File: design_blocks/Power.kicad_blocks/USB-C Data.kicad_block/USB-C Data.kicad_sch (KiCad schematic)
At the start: 7 parts, among them J12 USB_C_Receptacle_USB2.0_16P, U3 USBLC6-2P6

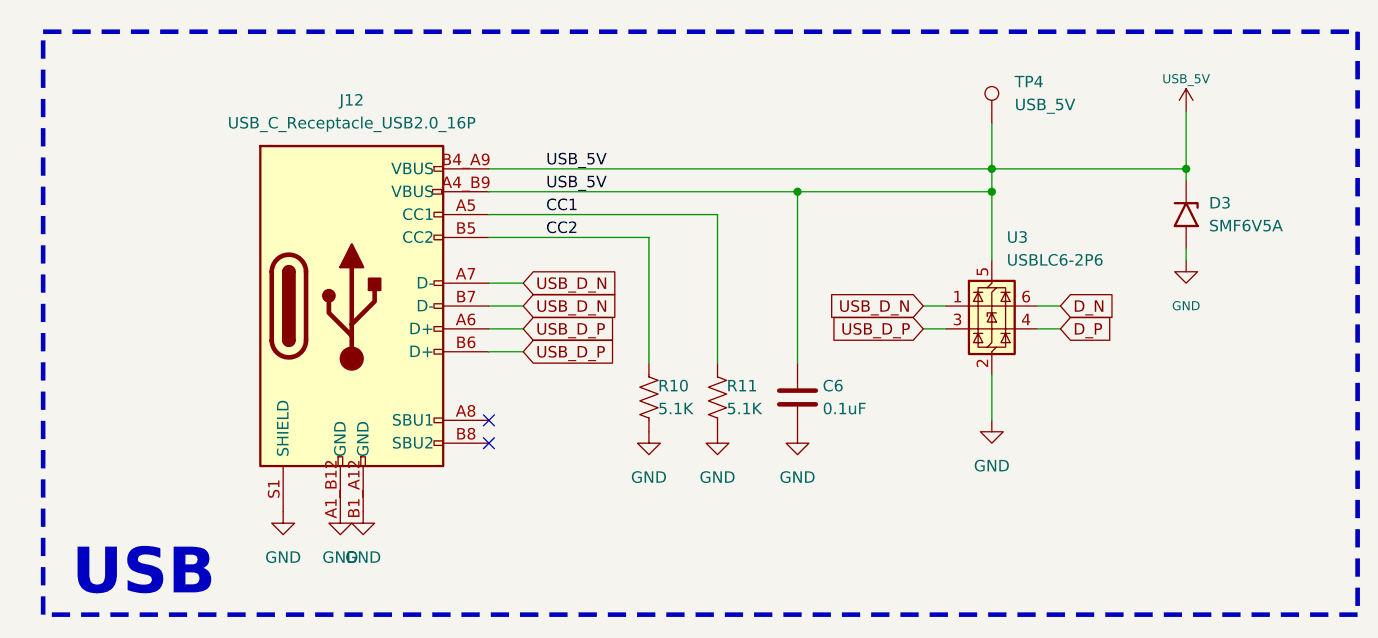
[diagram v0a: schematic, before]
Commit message: Moved stock parts to CRGM libraries
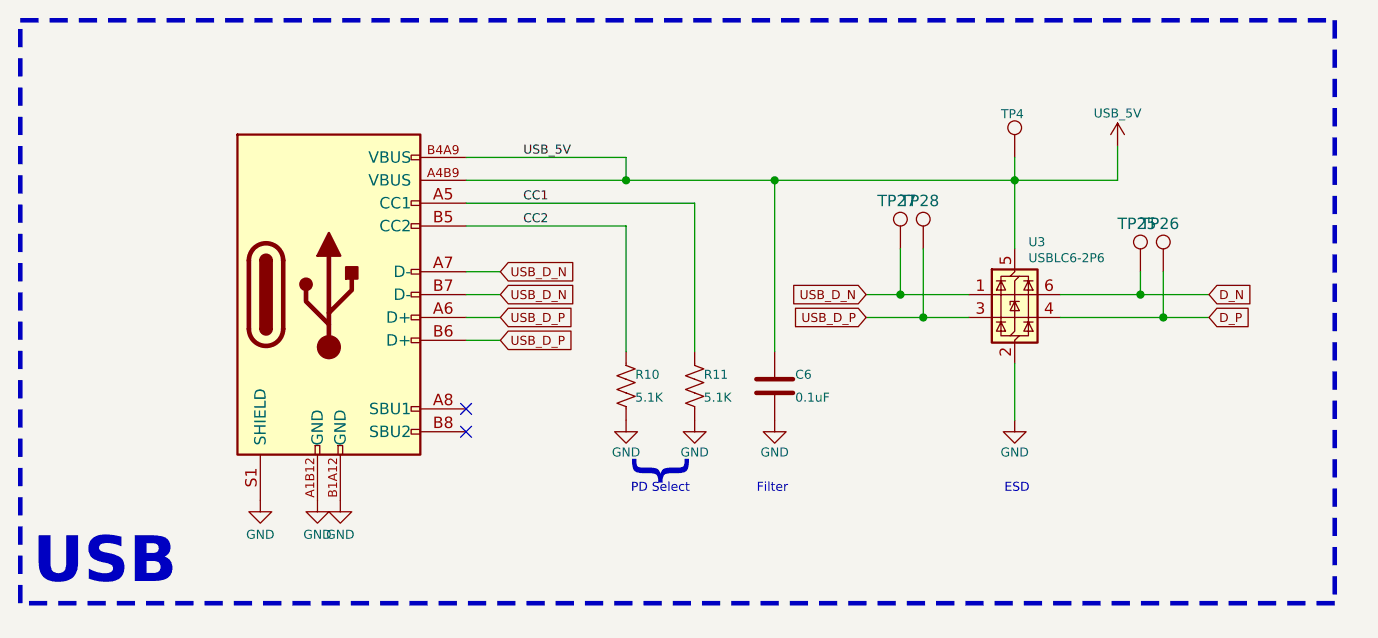
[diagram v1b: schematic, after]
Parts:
- removed D3: SMF6V5A, Diode_SMD:D_SOD-123F, symbol Diode:SMF6V5A
- removed J12: USB_C_Receptacle_USB2.0_16P, Connector_USB:USB_C_Receptacle_GCT_USB4105-xx-A_16P_TopMnt_Horizontal, symbol Connector:USB_C_Receptacle_USB2.0_16P
- added J2: USB_C_USB2.0_16P, CRGM Connector:GCT_USB4105-GF-A, symbol CRGM Connector:USB_C_USB2.0_16P
- added TP25, TP26, TP27, TP28: TP, CRGM Mechanical:TestPoint_Pad_D1.0mm, symbol Connector:TestPoint
- C6: Digikey (none) -> 1276-1005-2-ND; LCSC (none) -> C66501; LCSC_PN C66501 -> (none); MF Samsung -> (none); MN (none) -> Samsung; Mouser (none) -> 187-CL10B104KO8NNNC
- R10, R11: Digikey (none) -> 118-CR0603-JW-512ELFTR-ND; LCSC (none) -> C2907114; LCSC_PN C2907114 -> (none); MF FOJAN -> (none); MN (none) -> FOJAN; Mouser (none) -> 652-CR0603JW-512ELF
- TP4: value USB_5V -> TP; footprint TestPoint:TestPoint_Pad_D1.0mm -> CRGM Mechanical:TestPoint_Pad_D1.0mm; now left out of the parts list
- U3: Digikey (none) -> 497-5026-2-ND; LCSC (none) -> C2827693; LCSC_PN C2827693 -> (none); MF TECH PUBLIC -> (none); MN (none) -> TECH PUBLIC; Mouser (none) -> 511-USBLC6-2P6
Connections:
- net CC1: now also J2.A5 (CC1)
- net CC2: now also J2.B5 (CC2)
- net D_N: now also TP25.1
- net D_P: now also TP26.1
- net GND: now also J2.A1B12 (GND), J2.B1A12 (GND), J2.S1 (SHIELD)
- net USB_5V: now also J2.A4B9 (VBUS), J2.B4A9 (VBUS)
- net USB_D_N: now also J2.A7 (D-), J2.B7 (D-), TP27.1
- net USB_D_P: now also J2.A6 (D+), J2.B6 (D+), TP28.1
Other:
- note added: "ESD"
- note added: "Filter"
- note added: "PD Select"
- note added: "{"
- moved on the sheet: C6, R10, R11, TP4, U3
